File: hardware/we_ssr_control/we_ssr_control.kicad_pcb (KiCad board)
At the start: 2 copper layers, 65 x 90 mm, 28 parts, among them Q1 IRF4905, U1 WeMos_D1_mini, U2 ULN2803A

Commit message: WIP control connector changes
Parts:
- added H4: MountingHole_Pad, MountingHole:MountingHole_3.2mm_M3_Pad_Via, F.Cu at (55.0, 135.0)
- added JL1: Conn_01x02, Connector_PinHeader_1.00mm:PinHeader_1x02_P1.00mm_Vertical, F.Cu at (104.2, 64.5)
- S1: footprint SamacSys_Parts:1938MS -> We_control:1938MS
- moved H2 80.0 mm to (110.0, 55.0)
- moved H3 68.0 mm to (110.0, 135.0)
- moved H1 55.0 mm to (55.0, 55.0)
- moved #LOGO2 40.2 mm to (96.2, 111.2)
- moved #LOGO3 37.6 mm to (97.8, 121.3)
- moved #LOGO1 28.5 mm to (96.2, 132.3)
- moved LED1 24.7 mm to (110.1, 64.3), turned to 90 degrees
- moved S1 13.3 mm to (77.3, 132.4)
- moved RS8 11.9 mm to (87.0, 109.0)
- moved RS6 11.2 mm to (87.0, 105.4)
- moved RS3 10.9 mm to (87.0, 100.0)
- moved RL1 10.5 mm to (96.1, 63.5), turned to 0 degrees
- moved RS1 10.3 mm to (87.0, 96.4)
- moved C3 9.22 mm to (64.1, 113.2), turned to -135 degrees
- moved RS7 8.88 mm to (87.0, 107.2)
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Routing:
- net /a1: track 66.2 -> 39.1 mm
- net /a3: track 58.9 -> 38.4 mm
- net /a2: track 57.2 -> 38.7 mm
- net /a4: track 50.9 -> 38.1 mm
- net Net-(JCNTL1-Pad10): track 8.23 -> 20.4 mm
- net Net-(JCNTL1-Pad8): track 8.24 -> 20.0 mm
- net /a6: track 49.3 -> 37.5 mm
- net Net-(JCNTL1-Pad6): track 8.18 -> 19.8 mm
- net Net-(JCNTL1-Pad4): track 8.18 -> 19.4 mm
- net Net-(JL1-Pad2): track 2.67 -> 13.2 mm
- net /a5: track 47.3 -> 37.8 mm
- net Net-(U1-Pad7): track 38.3 -> 30.0 mm
- net Net-(JCNTL1-Pad9): track 10.2 -> 17.2 mm
- net Net-(JCNTL1-Pad5): track 10.2 -> 17.0 mm
- net Net-(U1-Pad6): track 38.3 -> 31.6 mm
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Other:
- outline, holes or cut-outs redrawn
- board text added: "0"
- board text added: "0 mm"
- board text added: "0.01 mm"
- board text added: "0.02"
- board text added: "0.07 mm"
- board text added: "1"
- board text added: "1.6 mm"
- board text added: "1.7600 mm"
- board text added: "3.3"
- board text added: "4.5"
- board text added: "B.Cu"
- board text added: "B.Mask"
- board text added: "B.Paste"
- board text added: "B.Silkscreen"
- board text added: "Bottom Silk Screen"
- board text added: "Bottom Solder Mask"
- board text added: "Bottom Solder Paste"
- board text added: "Color"
- board text added: "Dielectric 1"
- board text added: "Epsilon R"
- board text added: "F.Cu"
- board text added: "F.Mask"
- board text added: "F.Paste"
- board text added: "F.Silkscreen"
- board text added: "FR4"
- board text added: "Green"
- board text added: "Layer Name"
- board text added: "Licensed under CERN-OHL-W v2"
- board text added: "Liquid Ink"
- board text added: "Liquid Photo"
- board text added: "Loss Tangent"
- board text added: "Material"
- board text added: "Rev: 0.0.5"
- board text added: "Thickness (mm)"
- board text added: "Top Silk Screen"
- board text added: "Top Solder Mask"
- board text added: "Top Solder Paste"
- board text added: "Type"
- board text added: "White"
- board text added: "copper"
- board text added: "core"
- board text removed: "1.3600 mm"
- board text removed: "Rev: 0.0.4"

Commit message: WIP for updated layout
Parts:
- removed C3: 100n, Capacitor_SMD:C_0805_2012Metric
- removed H4: MountingHole_Pad, MountingHole:MountingHole_3.2mm_M3_Pad_Via
- removed U2: ULN2803A, Package_DIP:DIP-18_W7.62mm
- added FID1: Fiducial, Fiducial:Fiducial_0.5mm_Mask1mm, F.Cu at (55.0, 62.5)
- added FID2: Fiducial, Fiducial:Fiducial_0.5mm_Mask1mm, F.Cu at (110.0, 62.5)
- added FID3: Fiducial, Fiducial:Fiducial_0.5mm_Mask1mm, F.Cu at (110.0, 135.0)
- added JCNTL2: SHF-105-01-L-D-RA, dragon_mobile:SAMTEC_SHF-105-01-L-D-RA, F.Cu at (107.5, 108.0)
- added JS1: SolderJumper_3_Bridged12, Jumper:SolderJumper-3_P1.3mm_Bridged12_RoundedPad1.0x1.5mm_NumberLabels, B.Cu at (105.0, 95.0)
- added JS2: Conn_01x02, Connector_PinHeader_1.00mm:PinHeader_1x02_P1.00mm_Vertical, F.Cu at (102.0, 95.0)
- added QD1: 2N7002K, Package_TO_SOT_SMD:SOT-23, F.Cu at (86.0, 87.0)
- added QD2: 2N7002K, Package_TO_SOT_SMD:SOT-23, F.Cu at (86.0, 90.5)
- added QD3: 2N7002K, Package_TO_SOT_SMD:SOT-23, F.Cu at (86.0, 93.9)
- added QD4: 2N7002K, Package_TO_SOT_SMD:SOT-23, F.Cu at (86.0, 97.3)
- added QD5: 2N7002K, Package_TO_SOT_SMD:SOT-23, F.Cu at (75.5, 118.3)
- added QD6: 2N7002K, Package_TO_SOT_SMD:SOT-23, F.Cu at (75.5, 114.9)
- added QD7: 2N7002K, Package_TO_SOT_SMD:SOT-23, F.Cu at (75.5, 111.5)
- added QD8: 2N7002K, Package_TO_SOT_SMD:SOT-23, F.Cu at (75.5, 108.0)
- added QRCode1: GitHub URL, LOGO, B.Cu at (60.5, 112.8)
- #LOGO3: moved to B.Cu
- JCNTL1: value Conn_02x06_Odd_Even -> SHF-105-01-L-D-RA; footprint Connector_IDC:IDC-Header_2x06_P2.54mm_Horizontal -> dragon_mobile:SAMTEC_SHF-105-01-L-D-RA
- RS1, RS2, RS3, RS4: value 25 -> 270
- RS5: renamed from RS8; value 25 -> 270
- RS6: renamed from RS7; value 25 -> 270
- RS7: renamed from RS6; value 25 -> 270
- RS8: renamed from RS5; value 25 -> 270
- moved H2 97.1 mm to (55.0, 135.0)
- moved H3 40.0 mm to (110.0, 95.0)
- moved RS3 23.1 mm to (103.0, 83.3), turned to 0 degrees
- moved RS1 22.4 mm to (103.0, 80.7), turned to 0 degrees
- moved RS4 21.3 mm to (99.5, 84.5)
- moved RS2 20.4 mm to (99.5, 82.0)
- moved #LOGO1 16.6 mm to (102.5, 117.0)
- moved RS8 16.1 mm to (103.0, 105.5)
- moved RS6 16.0 mm to (103.0, 108.0)
- moved LED1 15.7 mm to (95.7, 58.0), turned to 180 degrees
- moved RS7 12.6 mm to (99.5, 106.7), turned to 0 degrees
- moved RS5 12.5 mm to (99.5, 109.3), turned to 0 degrees
- moved #LOGO3 11.3 mm to (90.7, 130.2), turned to 180 degrees
- moved S1 11.2 mm to (88.5, 132.3)
- moved #LOGO2 9.65 mm to (88.5, 117.0)
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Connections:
- JCNTL1 pad 1: +BATT -> Net-(JCNTL1-Pad1)
- JCNTL1 pad 10: Net-(JCNTL1-Pad10) -> GNDPWR
- JCNTL1 pad 2: +BATT -> GNDPWR
- JCNTL1 pad 4: Net-(JCNTL1-Pad4) -> GNDPWR
- JCNTL1 pad 6: Net-(JCNTL1-Pad6) -> GNDPWR
- JCNTL1 pad 8: Net-(JCNTL1-Pad8) -> GNDPWR
- RS1 pad 1: Net-(JCNTL1-Pad4) -> /a1
- RS1 pad 2: /a1 -> Net-(JCNTL1-Pad3)
- RS2 pad 2: Net-(JCNTL1-Pad3) -> Net-(JCNTL1-Pad5)
- RS3 pad 1: Net-(JCNTL1-Pad6) -> /a3
- RS3 pad 2: /a3 -> Net-(JCNTL1-Pad7)
- RS4 pad 2: Net-(JCNTL1-Pad5) -> Net-(JCNTL1-Pad9)
- RS5 pad 1: Net-(JCNTL1-Pad10) -> /a5
- RS5 pad 2: /a8 -> Net-(JCNTL2-Pad7)
- RS6 pad 1: /a7 -> /a6
- RS6 pad 2: Net-(JCNTL1-Pad9) -> Net-(JCNTL2-Pad5)
- RS7 pad 1: Net-(JCNTL1-Pad8) -> /a7
- RS7 pad 2: /a6 -> Net-(JCNTL2-Pad3)
- RS8 pad 1: /a5 -> /a8
- RS8 pad 2: Net-(JCNTL1-Pad7) -> Net-(JCNTL2-Pad1)
- S1 pad 13: /a5 -> /a8
- S1 pad 14: /a6 -> /a7
- S1 pad 15: /a7 -> /a6
- S1 pad 16: /a8 -> /a5
- U1 pad 1: (no net) -> unconnected-(U1-Pad1)
- U1 pad 11: Net-(U1-Pad11) -> /b1
- U1 pad 12: Net-(U1-Pad12) -> /b2
- U1 pad 13: Net-(U1-Pad13) -> /b3
- U1 pad 14: Net-(U1-Pad14) -> /b4
- U1 pad 15: (no net) -> unconnected-(U1-Pad15)
- U1 pad 16: (no net) -> unconnected-(U1-Pad16)
- U1 pad 2: (no net) -> unconnected-(U1-Pad2)
- U1 pad 4: Net-(U1-Pad4) -> /b8
- U1 pad 5: Net-(U1-Pad5) -> /b7
- U1 pad 6: Net-(U1-Pad6) -> /b6
- U1 pad 7: Net-(U1-Pad7) -> /b5
- U1 pad 8: (no net) -> unconnected-(U1-Pad8)
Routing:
- net +VDC: track 61.3 -> 10.5 mm, vias 1 -> 0
- net /b5: track 0.00 -> 49.0 mm
- net /b6: track 0.00 -> 48.1 mm
- net /b7: track 0.00 -> 47.1 mm
- net /b8: track 0.00 -> 46.3 mm
- net Net-(U1-Pad14): track 38.6 -> 0.00 mm
- net /b4: track 0.00 -> 37.1 mm
- net Net-(U1-Pad4): track 34.5 -> 0.00 mm
- net Net-(U1-Pad13): track 33.5 -> 0.00 mm
- net Net-(U1-Pad5): track 33.0 -> 0.00 mm
- net Net-(U1-Pad6): track 31.6 -> 0.00 mm
- net /b3: track 0.00 -> 30.3 mm
- net Net-(U1-Pad7): track 30.0 -> 0.00 mm
- net Net-(U1-Pad12): track 28.4 -> 0.00 mm
- net /a1: track 39.1 -> 64.2 mm, vias 1 -> 2
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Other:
- outline, holes or cut-outs redrawn
- board text added: "+"
- board text added: "+BATT a1 a2 a3 a4"
- board text added: "0.2000 mm / 0.1800 mm"
- board text added: "1.1600 mm"
- board text added: "JCNTL1"
- board text added: "JCNTL2"
- board text added: "Mounting holes are for M3 screws and should be drill at 2.5mm (#39) and tapped at .5mm threads. Additional support for the two corners without mounting holes may be needed in high vibration enviroments."
- board text added: "a1"
- board text added: "a2"
- board text added: "a3"
- board text added: "a4"
- board text added: "a5"
- board text added: "a6"
- board text added: "a7"
- board text added: "a8"
- board text added: "a8 a7 a6 a5 +BATT"
- board text added: "v0.0.8"
- board text removed: "0"
- board text removed: "0 mm"
- board text removed: "0.01 mm"
- board text removed: "0.02"
- board text removed: "0.07 mm"
- board text removed: "0.2000 mm / 0.0000 mm"
- board text removed: "1"
- board text removed: "1.6 mm"
- board text removed: "1.7600 mm"
- board text removed: "3.3"
- board text removed: "4.5"
- board text removed: "B.Cu"
- board text removed: "B.Mask"
- board text removed: "B.Paste"
- board text removed: "B.Silkscreen"
- board text removed: "Bottom Silk Screen"
- board text removed: "Bottom Solder Mask"
- board text removed: "Bottom Solder Paste"
- board text removed: "Color"
- board text removed: "Dielectric 1"
- board text removed: "Epsilon R"
- board text removed: "F.Cu"
- board text removed: "F.Mask"
- board text removed: "F.Paste"
- board text removed: "F.Silkscreen"
- board text removed: "FR4"
- board text removed: "Green"
- board text removed: "Layer Name"
- board text removed: "Liquid Ink"
- board text removed: "Liquid Photo"
- board text removed: "Loss Tangent"
- board text removed: "Material"
- board text removed: "Rev: 0.0.5"
- board text removed: "Thickness (mm)"
- board text removed: "Top Silk Screen"
- board text removed: "Top Solder Mask"
- board text removed: "Top Solder Paste"
- board text removed: "Type"
- board text removed: "White"
- board text removed: "copper"
- board text removed: "core"
- board text removed: "https://github.com/dragon-mobile/we_ssr_control"

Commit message: Minor updates for v0.0.9
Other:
- board text added: "H1"
- board text added: "H2"
- board text added: "H3"
- board text added: "v0.0.9"
- board text removed: "+"
- board text removed: "v0.0.8"

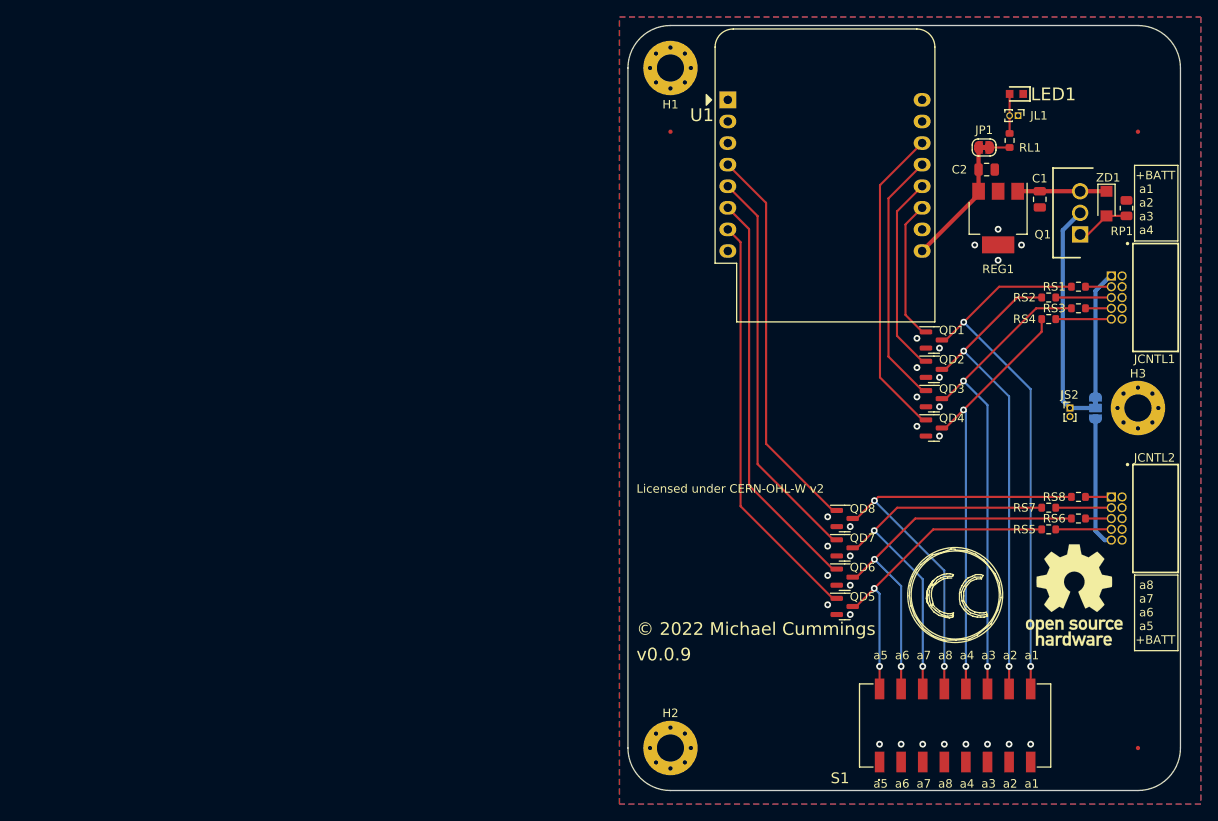
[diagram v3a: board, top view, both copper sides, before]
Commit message: Changed schematic to hierarchical style with mutliple sheets
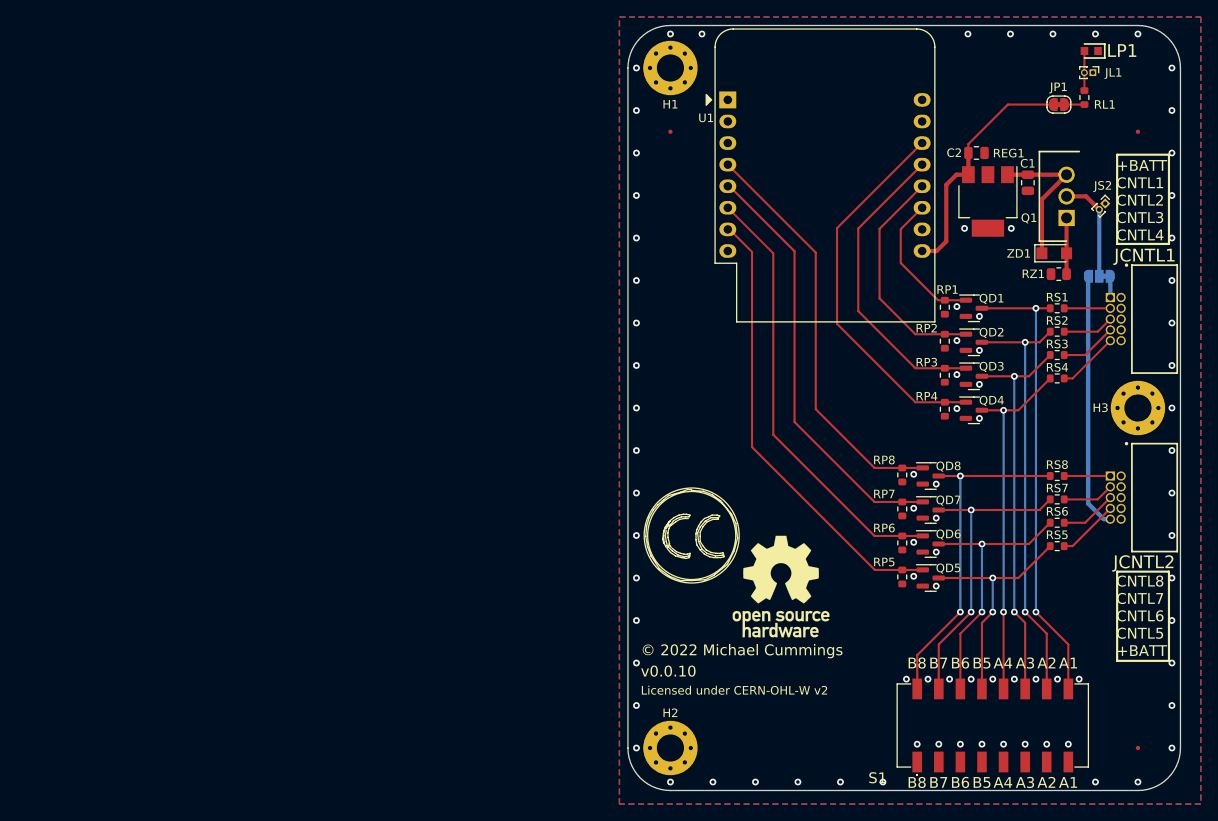
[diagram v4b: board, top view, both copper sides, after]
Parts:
- removed LED1: LTST-C190KGKT, dragon_mobile:LEDC1608X80N
- added LP1: LTST-C190KGKT, dragon_mobile:LEDC1608X80N, F.Cu at (104.5, 53.0)
- added RP2: 10k, Resistor_SMD:R_0603_1608Metric, F.Cu at (87.3, 87.1)
- added RP3: 10k, Resistor_SMD:R_0603_1608Metric, F.Cu at (87.3, 91.1)
- added RP4: 10k, Resistor_SMD:R_0603_1608Metric, F.Cu at (87.3, 95.1)
- added RP5: 10k, Resistor_SMD:R_0603_1608Metric, F.Cu at (82.3, 114.9)
- added RP6: 10k, Resistor_SMD:R_0603_1608Metric, F.Cu at (82.3, 110.9)
- added RP7: 10k, Resistor_SMD:R_0603_1608Metric, F.Cu at (82.3, 106.9)
- added RP8: 10k, Resistor_SMD:R_0603_1608Metric, F.Cu at (82.3, 102.9)
- added RZ1: 100k, Resistor_SMD:R_0805_2012Metric, F.Cu at (100.7, 79.2)
- Q1: value IRF4905 -> IRF4905PBF
- RP1: value 100k -> 10k; footprint Resistor_SMD:R_0805_2012Metric -> Resistor_SMD:R_0603_1608Metric
- S1: footprint We_control:1938MS -> dragon_mobile:1938MS
- U1: footprint Module:WEMOS_D1_mini_light -> dragon_mobile:WEMOS_D1_mini_light
- ZD1: footprint Diode_SMD:D_SMF -> dragon_mobile:BZD27C10P-M3-08
- moved #LOGO1 34.5 mm to (68.0, 116.0)
- moved #LOGO2 31.8 mm to (57.5, 110.0)
- moved JS2 24.4 mm to (106.2, 70.9), turned to -45 degrees
- moved RP1 24.3 mm to (87.3, 83.1), turned to -90 degrees
- moved JS1 15.5 mm to (105.5, 79.5), turned to 180 degrees
- moved QD8 11.3 mm to (85.6, 103.0)
- moved QD7 11.1 mm to (85.6, 107.0)
- moved QD6 10.8 mm to (85.6, 111.0)
- moved QD5 10.7 mm to (85.6, 115.0)
- moved JL1 10.1 mm to (104.7, 55.5)
- moved JP1 10.1 mm to (100.7, 59.3)
- moved RL1 10.1 mm to (103.7, 58.5)
- moved ZD1 8.49 mm to (100.2, 76.8), turned to 0 degrees
- moved RS4 7.05 mm to (100.5, 91.5)
- moved RS3 6.04 mm to (100.5, 88.8)
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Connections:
- net /a1 renamed /Control Out/BANK_A.CNTL1
- net /a2 renamed /Control Out/BANK_A.CNTL2
- net /a3 renamed /Control Out/BANK_A.CNTL3
- net /a4 renamed /Control Out/BANK_A.CNTL4
- net /b2 renamed /WeMOS Control/IO2
- net /b3 renamed /WeMOS Control/IO3
- net /b4 renamed /WeMOS Control/IO4
- net /b5 renamed /WeMOS Control/IO5
- net /b6 renamed /WeMOS Control/IO6
- net /b7 renamed /WeMOS Control/IO7
- net /b8 renamed /WeMOS Control/IO8
- net Net-(JCNTL1-Pad1) renamed /Control Out/PwrIn1
- net Net-(JCNTL1-Pad3) renamed /Control Out/a1o
- net Net-(JCNTL1-Pad5) renamed /Control Out/a2o
- net Net-(JCNTL1-Pad7) renamed /Control Out/a3o
- net Net-(JCNTL1-Pad9) renamed /Control Out/a4o
- net Net-(JCNTL2-Pad1) renamed /Control Out/a8o
- net Net-(JCNTL2-Pad3) renamed /Control Out/a7o
- net Net-(JCNTL2-Pad5) renamed /Control Out/a6o
- net Net-(JCNTL2-Pad7) renamed /Control Out/a5o
- net Net-(JCNTL2-Pad9) renamed /Control Out/PwrIn2
- JS2 pad 1: +BATT -> GNDPWR
- JS2 pad 2: GNDPWR -> +BATT
- QD1 pad 1: /b1 -> /WeMOS Control/IO1
- QD5 pad 3: /a5 -> /Control Out/BANK_B.CNTL5
- QD6 pad 3: /a6 -> /Control Out/BANK_B.CNTL6
- QD7 pad 3: /a7 -> /Control Out/BANK_B.CNTL7
- QD8 pad 3: /a8 -> /Control Out/BANK_B.CNTL8
- RP1 pad 1: Net-(Q1-Pad1) -> /WeMOS Control/IO1
- RS5 pad 1: /a5 -> /Control Out/BANK_B.CNTL5
- RS6 pad 1: /a6 -> /Control Out/BANK_B.CNTL6
- RS7 pad 1: /a7 -> /Control Out/BANK_B.CNTL7
- RS8 pad 1: /a8 -> /Control Out/BANK_B.CNTL8
- S1 pad 13: /a8 -> /Control Out/BANK_B.CNTL5
- S1 pad 14: /a7 -> /Control Out/BANK_B.CNTL6
- S1 pad 15: /a6 -> /Control Out/BANK_B.CNTL7
- S1 pad 16: /a5 -> /Control Out/BANK_B.CNTL8
- U1 pad 1: unconnected-(U1-Pad1) -> (no net)
- U1 pad 11: /b1 -> /WeMOS Control/IO1
- U1 pad 15: unconnected-(U1-Pad15) -> (no net)
- U1 pad 16: unconnected-(U1-Pad16) -> (no net)
- U1 pad 2: unconnected-(U1-Pad2) -> (no net)
- U1 pad 8: unconnected-(U1-Pad8) -> (no net)
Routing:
- net /a8: track 52.3 -> 0.00 mm, vias 2 -> 0
- net /a7: track 45.2 -> 0.00 mm, vias 2 -> 0
- net /a6: track 45.1 -> 0.00 mm, vias 2 -> 0
- net /Control Out/BANK_B.CNTL8: track 0.00 -> 40.3 mm, vias 0 -> 2
- net /a5: track 38.1 -> 0.00 mm, vias 2 -> 0
- net /Control Out/BANK_B.CNTL7: track 0.00 -> 36.3 mm, vias 0 -> 2
- net /Control Out/BANK_B.CNTL6: track 0.00 -> 32.3 mm, vias 0 -> 2
- net /Control Out/BANK_B.CNTL5: track 0.00 -> 28.2 mm, vias 0 -> 2
- net /WeMOS Control/IO1: track 0.00 -> 17.0 mm
- net /b1: track 16.7 -> 0.00 mm
- net +BATT: track 27.2 -> 12.3 mm
- net /Control Out/PwrIn2: track 15.5 -> 30.1 mm
- net +5V: track 14.9 -> 28.6 mm
- net /Control Out/PwrIn1: track 15.1 -> 2.50 mm
- net /Control Out/BANK_A.CNTL3: track 57.0 -> 46.4 mm
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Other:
- board text added: "+BATT CNTL1 CNTL2 CNTL3 CNTL4"
- board text added: "A1"
- board text added: "A2"
- board text added: "A3"
- board text added: "A4"
- board text added: "B5"
- board text added: "B6"
- board text added: "B7"
- board text added: "B8"
- board text added: "CNTL8 CNTL7 CNTL6 CNTL5 +BATT"
- board text added: "v0.0.10"
- board text removed: "+BATT a1 a2 a3 a4"
- board text removed: "JCNTL1"
- board text removed: "JCNTL2"
- board text removed: "a1"
- board text removed: "a2"
- board text removed: "a3"
- board text removed: "a4"
- board text removed: "a5"
- board text removed: "a6"
- board text removed: "a7"
- board text removed: "a8"
- board text removed: "a8 a7 a6 a5 +BATT"
- board text removed: "v0.0.9"
